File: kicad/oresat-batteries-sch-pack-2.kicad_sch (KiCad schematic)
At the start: 84 parts, among them Q11 SI7625DN-T1-GE3, Q23 Si7336ADP, Q24 PM45VEN, Q25 PM45VEN, Q26 PM45VEN, Q27 PM45VEN, Q30 SI7625DN-T1-GE3, Q31 SI7625DN-T1-GE3, Q32 NTR4101, Q33 NTR4101, Q34 SI7625DN-T1-GE3, Q35 SI7625DN-T1-GE3, Q36 SI7625DN-T1-GE3, Q37 SI7625DN-T1-GE3, U13 S-8209AAA-T8T1U, U14 S-8209AAA-T8T1U, U15 LTC4412, U16 LTC4412, U17 MAX17205G

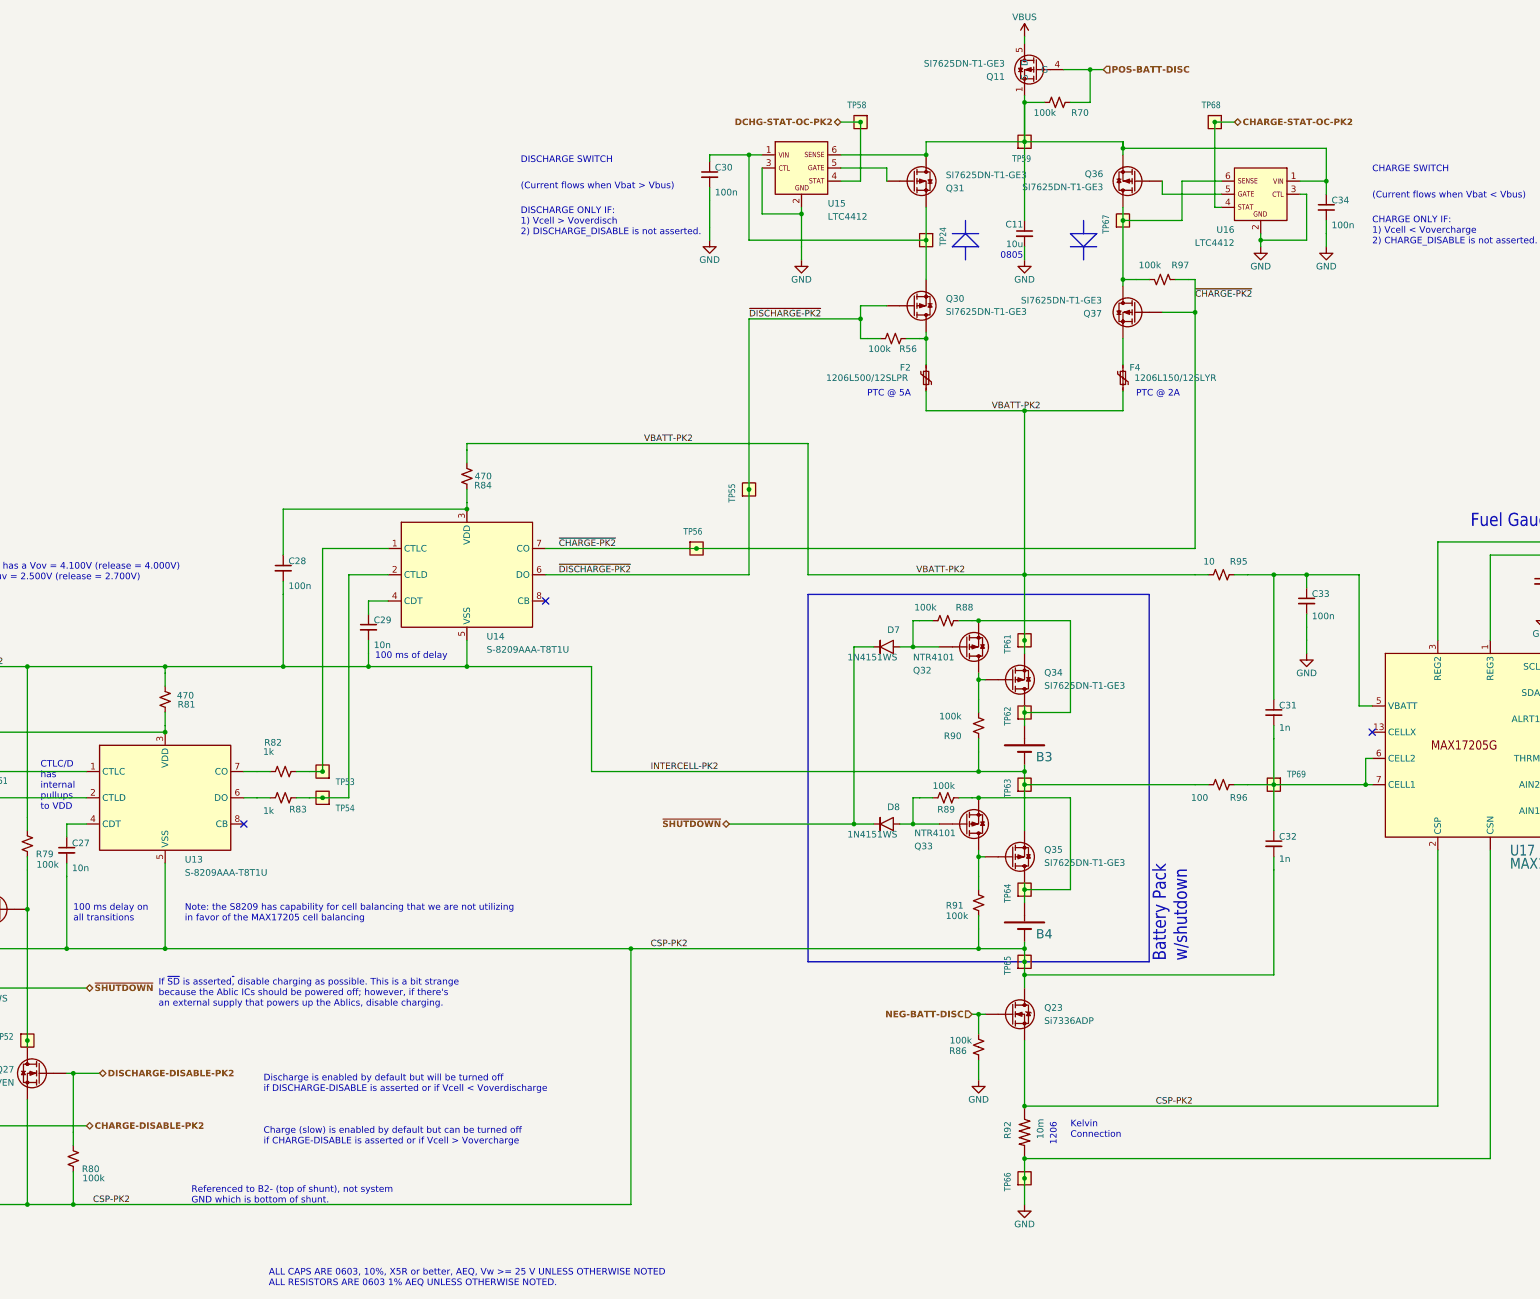
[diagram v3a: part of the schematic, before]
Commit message: Progress on v4
Figure out to bypass negative battery cutoff with 10k to make sure that nSHUTDOWN always works. Lots of moving around (it's tight), finally got pack 1 done. Working on the Pack 2.
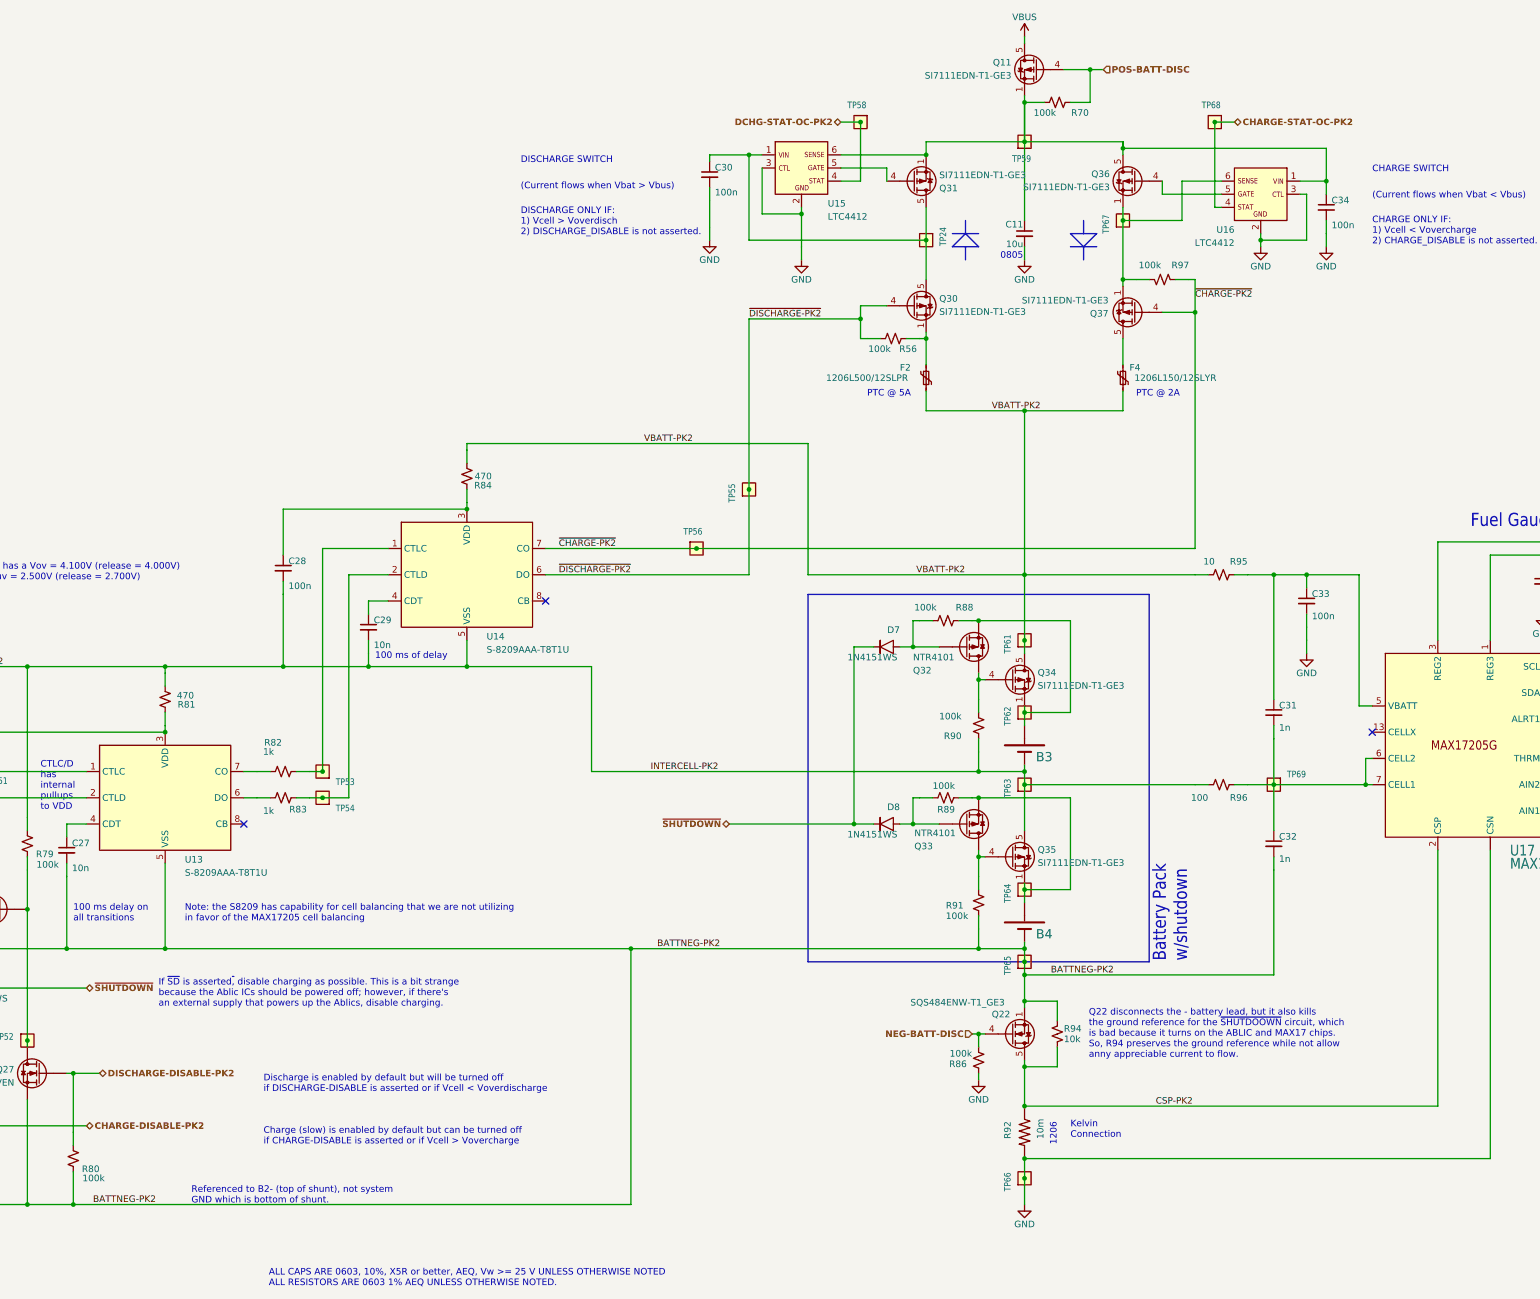
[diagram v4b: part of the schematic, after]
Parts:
- removed Q23: Si7336ADP, Package_SO:PowerPAK_SO-8_Single, symbol Transistor_FET:Si7336ADP
- added Q22: SQS484ENW-T1_GE3, Package_SO:Vishay_PowerPAK_1212-8_Single, symbol Transistor_FET:SiS454DN
- added R94: 10k, oresat-batteries:.0603-C-NOSILK, symbol Device:R_Small_US
- Q11, Q30, Q31, Q34, Q35, Q36, Q37: value SI7625DN-T1-GE3 -> SI7111EDN-T1-GE3; footprint oresat-batteries:POWERPAK-1212-8 -> Package_SO:Vishay_PowerPAK_1212-8_Single; symbol oresat-batteries-eagle-import:Q-VISHAY-MOSFET-PCH-POWERPAK-1212-8 -> Transistor_FET:SiS443DN
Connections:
- net CSP-PK2: now also Q22.5 (D), R94.1; no longer B4.2 (NEG), C26.2, C27.2, C32.2, Q24.2 (S), Q25.2 (S), Q26.2 (S), Q27.2 (S), R77.1, R80.1, R91.2, TP65.1, U13.5 (VSS)
- net INTERCELL-PK2: now also Q35.5 (D); no longer Q35.1 (S)
- net NEG-BATT-DISC: now also Q22.4 (G)
- net VBATT-PK2: now also Q34.5 (D); no longer Q34.1 (S)
- net at C11.1, C34.1, Q11.1 (S)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: now also Q11.2 (S), Q11.3 (S), Q31.1 (S), Q31.2 (S), Q31.3 (S), Q36.5 (D); no longer Q31.5 (D), Q36.1 (S)
- net at F2.1, R56.2: now also Q30.1 (S), Q30.2 (S), Q30.3 (S); no longer Q30.5 (D)
- net at C30.1, TP24.1, U15.1 (VIN): now also Q30.5 (D), Q31.5 (D); no longer Q30.1 (S), Q31.1 (S)
- net at B3.1 (POS), Q32.2 (S), R88.2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: now also Q34.1 (S), Q34.2 (S), Q34.3 (S); no longer Q34.5 (D)
- net at B4.1 (POS), Q33.2 (S), R89.1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: now also Q35.1 (S), Q35.2 (S), Q35.3 (S); no longer Q35.5 (D)
- net at R97.1, TP67.1, U16.6 (SENSE): now also Q36.1 (S), Q36.2 (S), Q36.3 (S), Q37.1 (S), Q37.2 (S), Q37.3 (S); no longer Q36.5 (D), Q37.5 (D)
- net at F4.1: now also Q37.5 (D); no longer Q37.1 (S)
- new net BATTNEG-PK2: B4.2 (NEG), C26.2, C27.2, C32.2, Q22.1 (S), Q22.2 (S), Q22.3 (S), Q24.2 (S), Q25.2 (S), Q26.2 (S), Q27.2 (S), R77.1, R80.1, R91.2, R94.2, TP65.1, U13.5 (VSS)
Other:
- note added: "Q22 disconnects the - battery lead, but it also kills the ground reference for the ~{SHUTDOOWN} circuit, which is bad because it turns on the ABLIC and MAX17 chips. So, R94 preserves the ground reference while not allow anny appreciable current to flow."
- moved on the sheet: R86
